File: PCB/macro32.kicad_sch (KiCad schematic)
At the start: 55 parts, among them J1 USB_C_Receptacle_USB2.0_16P, SW1 RST, SW2 boot, SW3 RotaryEncoder_Switch, SW4 RotaryEncoder_Switch, U1 STM32F072C8Tx, U2 USBLC6-2P6, U3 XC6206PxxxMR, U4 74AHC1G125

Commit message: V1.1
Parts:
- removed D1, D10, D11, D16, D17, D18, D2, D3, D4, D5, D6, D7, D8, D9: Diode, ScottoKeebs_Components:Diode_SOD-123, symbol ScottoKeebs:Placeholder_Diode
- removed S1, S10, S11, S12, S2, S3, S4, S5, S6, S7, S8, S9: Keyswitch, ScottoKeebs_Hotswap:Hotswap_MX_1.00u, symbol ScottoKeebs:Placeholder_Keyswitch
- removed SW3, SW4: RotaryEncoder_Switch, kbd:keyswitch_cherrymx_hotswap_1u_rotary_encoder_ec12, symbol Device:RotaryEncoder_Switch
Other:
- added sheet Switch Matrix (Switch_Matrix.kicad_sch)

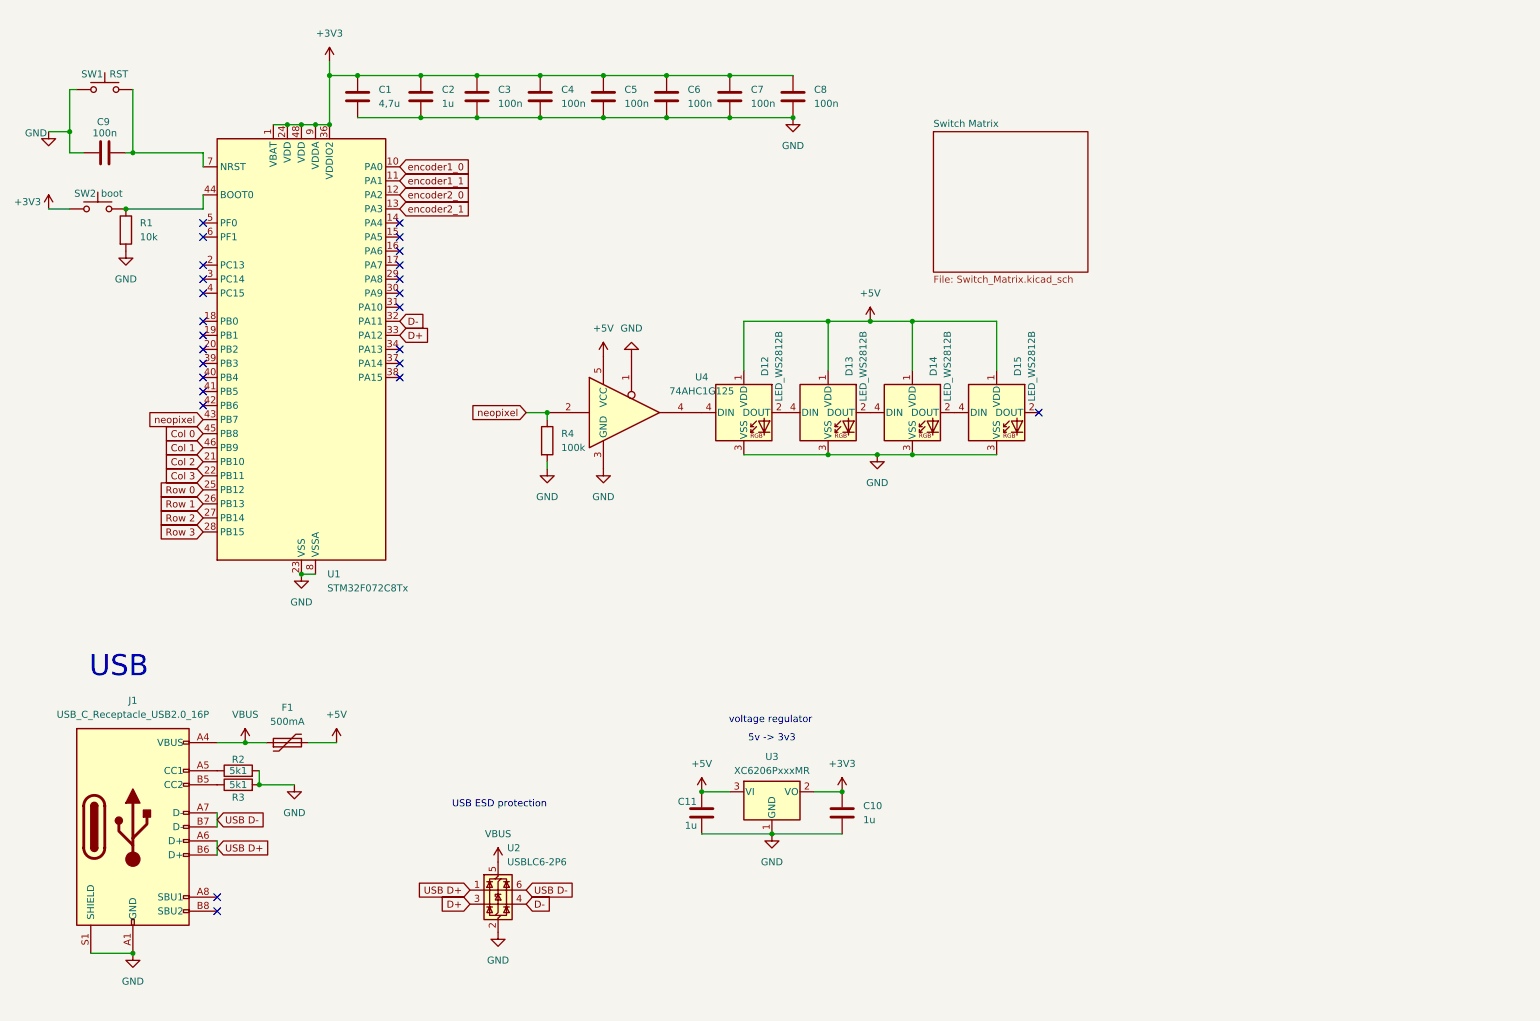
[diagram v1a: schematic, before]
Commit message: Schema for V2 Did some cleanup and seperated the switch matrix to it's own file fixes #1
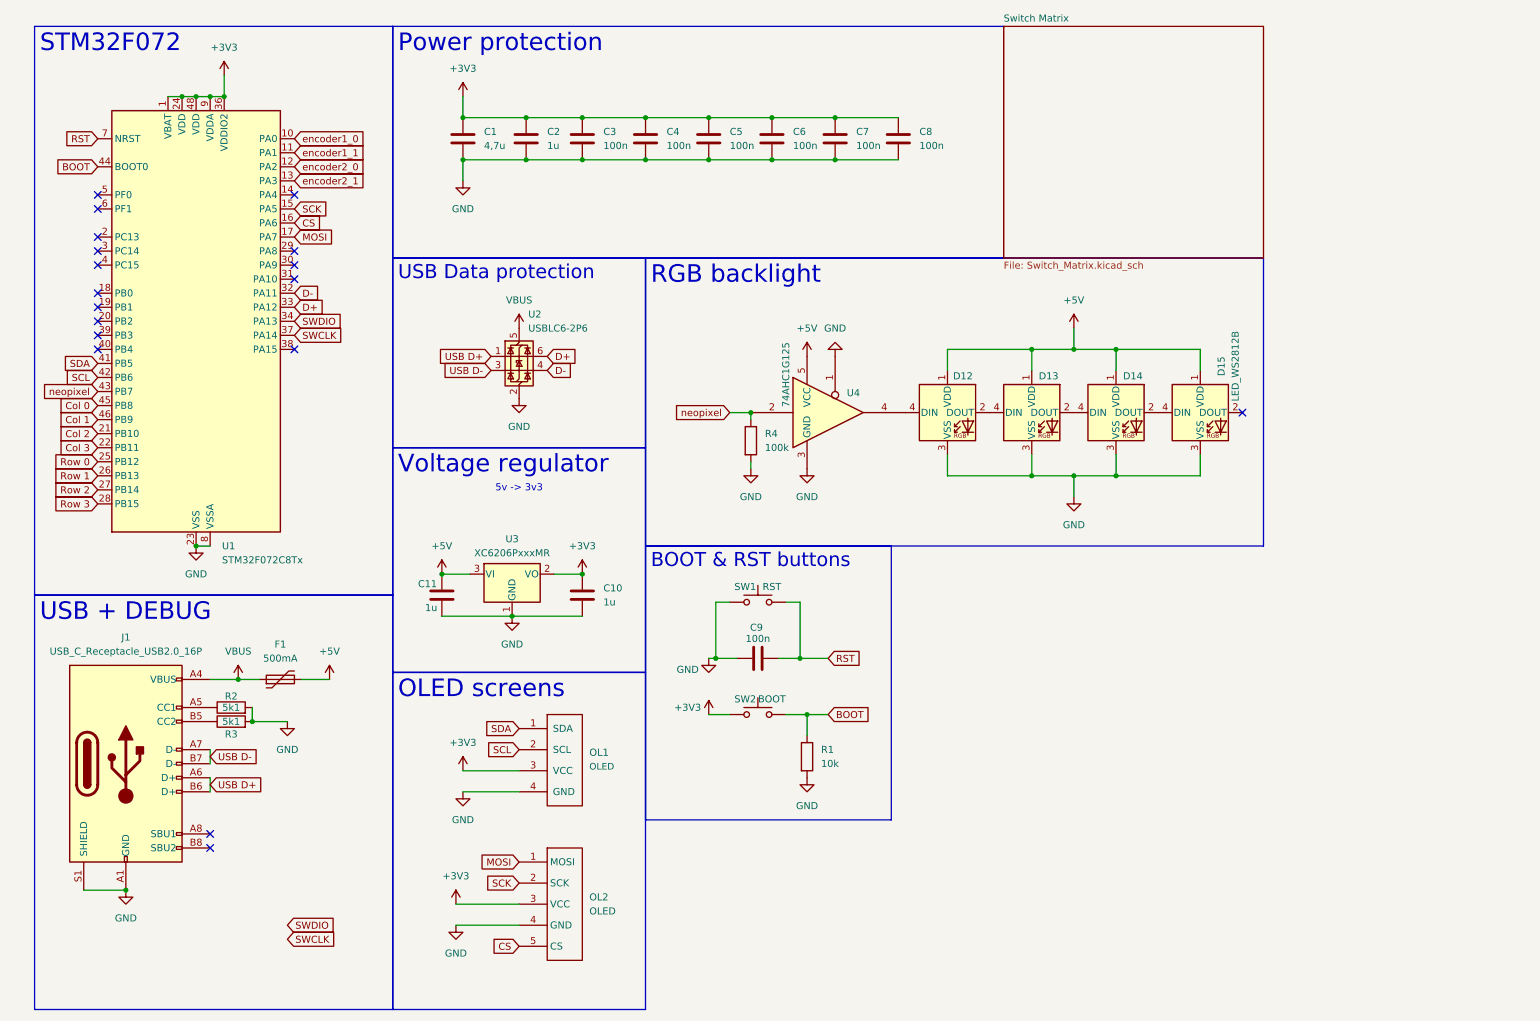
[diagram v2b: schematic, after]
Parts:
- added OL1: OLED, kbd:OLED, symbol kbd:OLED
- added OL2: OLED, kbd:OLED_SPI, symbol kbd:OLED_SPI
- SW2: value boot -> BOOT
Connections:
- net +3V3: now also OL1.3 (VCC), OL2.3 (VCC)
- net D+: now also U2.6 (I/O1); no longer U2.3 (I/O2)
- net GND: now also OL1.4 (GND), OL2.4 (GND)
- net USB D-: now also U2.3 (I/O2); no longer U2.6 (I/O1)
- net RST: now reaches C9.2, SW1.2, U1.7 (NRST)
- net SCK: now reaches U1.15 (PA5)
- net SCK: now also OL2.2 (SCK)
- net CS: now reaches U1.16 (PA6)
- net CS: now also OL2.5 (CS)
- net MOSI: now reaches U1.17 (PA7)
- net MOSI: now also OL2.1 (MOSI)
- net SWDIO: now reaches U1.34 (PA13)
- net SWCLK: now reaches U1.37 (PA14)
- net SDA: now reaches U1.41 (PB5)
- net SDA: now also OL1.1 (SDA)
- net SCL: now reaches U1.42 (PB6)
- net SCL: now also OL1.2 (SCL)
- net BOOT: now reaches R1.1, SW2.2, U1.44 (BOOT0)
- no-connect marks 25 -> 18
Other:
- note removed: "USB"
- note removed: "USB ESD protection"
- note removed: "voltage regulator"
- company: (none) -> KillrOfLife
- title: (none) -> Macro32
- moved on the sheet: C1, C10, C11, C2, C3, C4, C5, C6, C7, C8, C9, D12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

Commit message: Adjust PCB layout and added magnetic connector for modularity
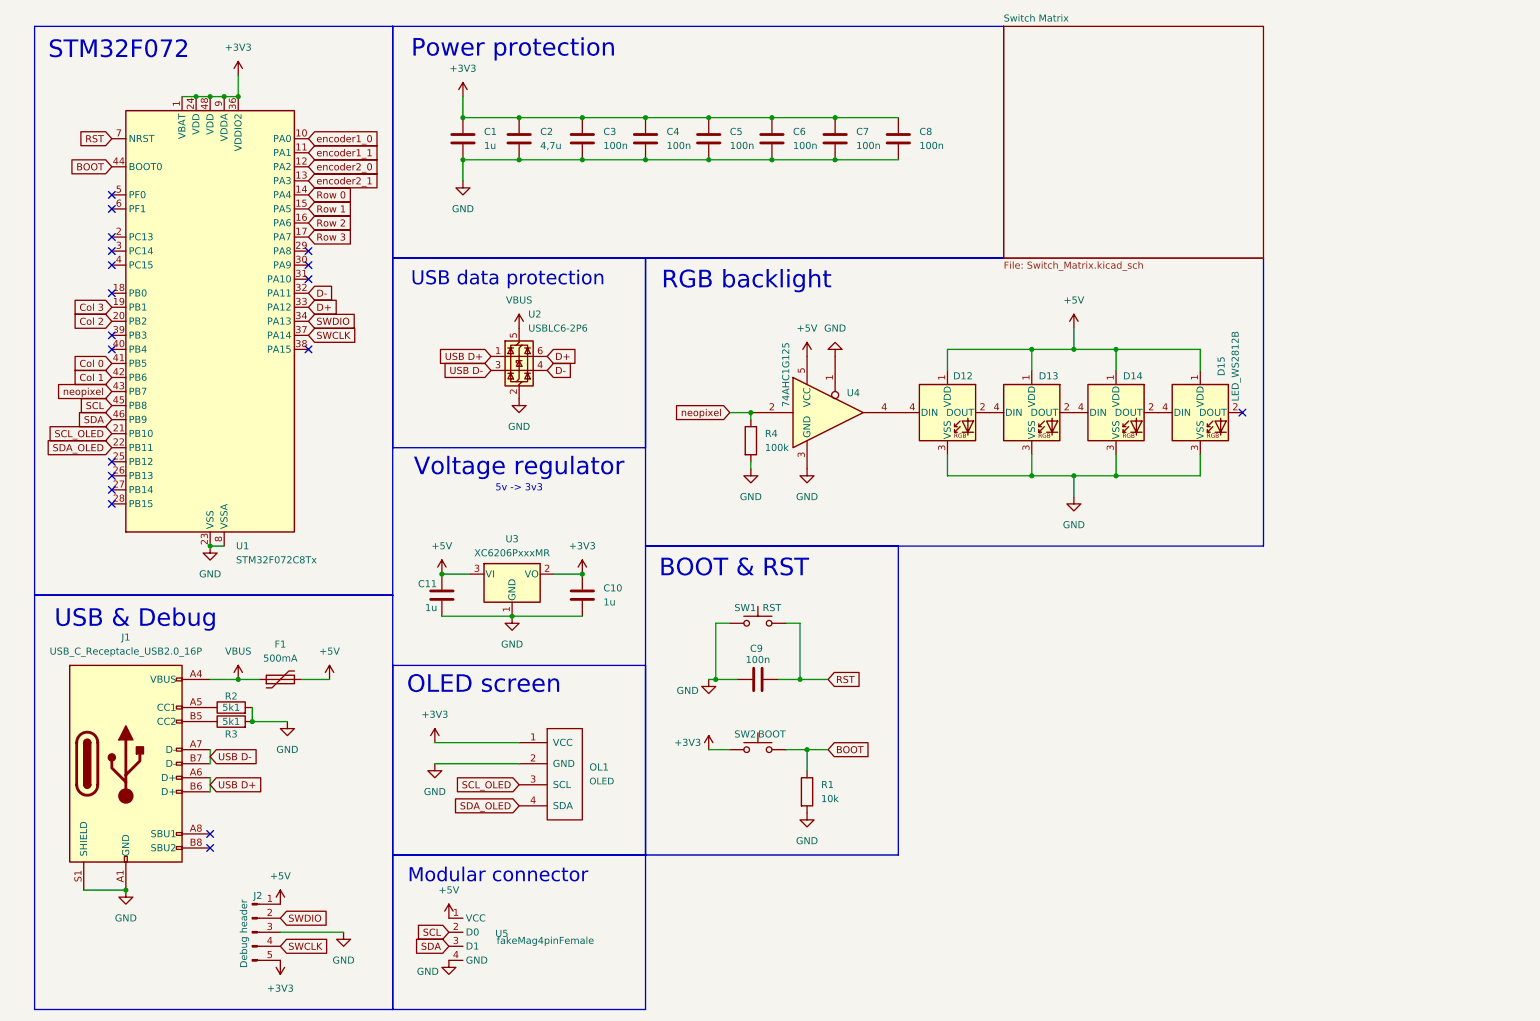
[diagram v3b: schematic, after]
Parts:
- removed OL2: OLED, kbd:OLED_SPI, symbol kbd:OLED_SPI
- added J2: Debug header, Connector_PinHeader_2.54mm:PinHeader_1x05_P2.54mm_Vertical, symbol Connector:Conn_01x05_Pin
- added U5: fakeMag4pinFemale, Library:fakemag4pin90degFemale, symbol New_Library:fakeMag4pinFemale
- OL1: footprint kbd:OLED -> ScottoKeebs_Components:OLED_128x64
- renumbered C2 to C1, C1 to C2
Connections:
- net CS is gone; now on net Row 2: U1.16 (PA6)
- net MOSI is gone; now on net Row 3: U1.17 (PA7)
- net SCK is gone; now on net Row 1: U1.15 (PA5)
- net +3V3: now also OL1.1 (VCC), J2.5 (Pin_5); no longer OL1.3 (VCC)
- net +5V: now also J2.1 (Pin_1), U5.1 (VCC)
- net Col 0: now also U1.41 (PB5); no longer U1.45 (PB8)
- net Col 1: now also U1.42 (PB6); no longer U1.46 (PB9)
- net Col 2: now also U1.20 (PB2); no longer U1.21 (PB10)
- net Col 3: now also U1.19 (PB1); no longer U1.22 (PB11)
- net GND: now also OL1.2 (GND), J2.3 (Pin_3), U5.4 (GND); no longer OL1.4 (GND)
- net Row 0: now also U1.14 (PA4); no longer U1.25 (PB12)
- net Row 1: no longer U1.26 (PB13)
- net Row 2: no longer U1.27 (PB14)
- net Row 3: no longer U1.28 (PB15)
- net SCL: now also U1.45 (PB8), U5.2 (D0); no longer OL1.2 (SCL), U1.42 (PB6)
- net SDA: now also U1.46 (PB9), U5.3 (D1); no longer OL1.1 (SDA), U1.41 (PB5)
- net SWCLK: now also J2.4 (Pin_4)
- net SWDIO: now also J2.2 (Pin_2)
- new net SCL_OLED: OL1.3 (SCL), U1.21 (PB10)
- new net SDA_OLED: OL1.4 (SDA), U1.22 (PB11)
- no-connect marks 18 -> 19
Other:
- note added: "BOOT & RST"
- note added: "Modular connector"
- note added: "OLED screen"
- note added: "Power protection"
- note added: "RGB backlight"
- note added: "STM32F072"
- note added: "USB & Debug"
- note added: "USB data protection"
- note added: "Voltage regulator"
- moved on the sheet: C1, C2, C9, OL1, R1, SW1, SW2, U1
